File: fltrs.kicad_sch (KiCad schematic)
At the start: 55 parts, among them U3 CPC1117N, U4 MCP6002, U5 MCP4451-503-ST, U6 MCP6002, U7 MCP6002

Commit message: initial commit, not complete.
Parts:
- C12, C14, C15, C16, C17, C18, C19, C20, C21, C22, C23, C24, C25, C29, C30, C31, C32, C33, C35: footprint Capacitor_SMD:C_0402_1005Metric -> Capacitor_SMD:C_0603_1608Metric_Pad1.08x0.95mm_HandSolder
- R10, R11, R12, R13, R14, R15, R16, R17, R18, R19, R20, R21, R22, R23, R25, R26, R27, R28, R6, R7, R8, R9: footprint Resistor_SMD:R_0402_1005Metric -> Resistor_SMD:R_0603_1608Metric_Pad0.98x0.95mm_HandSolder
- R24: footprint Resistor_SMD:R_0603_1608Metric -> Resistor_SMD:R_0603_1608Metric_Pad0.98x0.95mm_HandSolder
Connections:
- net +3V3: no longer R26.1
- new net VDDA: R26.1

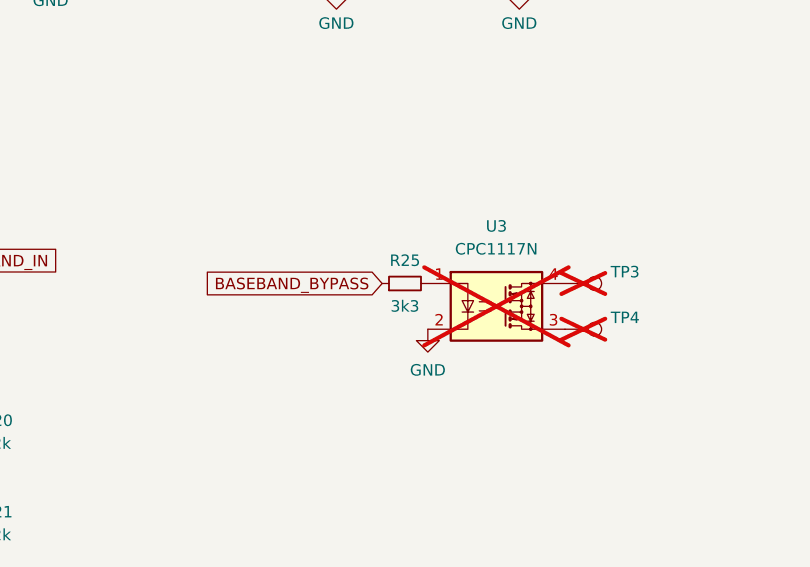
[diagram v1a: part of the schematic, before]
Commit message: PCB shape is created. Most of routing done.
Todo: assign pins for radio control signals.
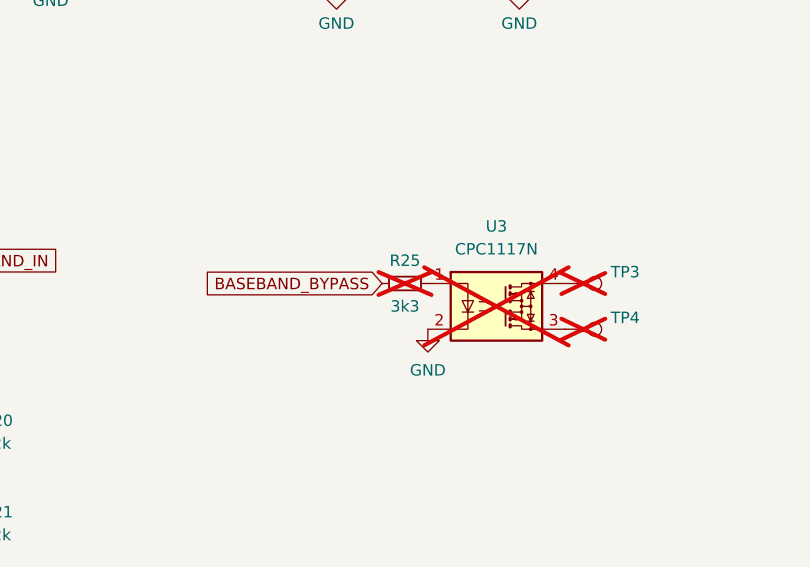
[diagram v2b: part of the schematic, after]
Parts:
- R25: now not fitted; now left out of the parts list
- U3: now left out of the parts list
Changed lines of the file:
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@@
 		(at 218.44 128.27 0)
 		(unit 1)
-		(exclude_from_sim no)
-		(in_bom yes)
-		(on_board yes)
+		(exclude_from_sim yes)
+		(in_bom no)
+		(on_board no)
 		(dnp yes)
 		(fields_autoplaced yes)
@@
 		(exclude_from_sim no)
 		(in_bom no)
-		(on_board yes)
+		(on_board no)
 		(dnp yes)
 		(fields_autoplaced yes)
@@
 		(exclude_from_sim no)
 		(in_bom no)
-		(on_board yes)
+		(on_board no)
 		(dnp yes)
 		(fields_autoplaced yes)
@@
 		(at 208.28 125.73 90)
 		(unit 1)
-		(exclude_from_sim no)
-		(in_bom yes)
-		(on_board yes)
-		(dnp no)
+		(exclude_from_sim yes)
+		(in_bom no)
+		(on_board no)
+		(dnp yes)
 		(property "Reference" "R25"
 			(at 208.28 123.19 90)
